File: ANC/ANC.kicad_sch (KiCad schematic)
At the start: 67 parts, among them J1 Screw_Terminal_01x04, J10 Conn_01x03, J11 Conn_01x03, J12 Conn_01x03, J13 Conn_01x03, J3 SJ2-35894B-SMT-TR, J5 Conn_01x04, J7 Conn_01x04, J8 Conn_01x04, J9 Conn_01x04, U1 ICS-40730, U2 MAX98090AETL_T, U3 ICS-40730, U4 CMM-3729AB-38308-TR, U5 CMM-3729AB-38308-TR, U6 TLV172IDCK, U7 TLV172IDCK, Y1 ASE-12.288MHZ-LC-T, x1 0, x2 0

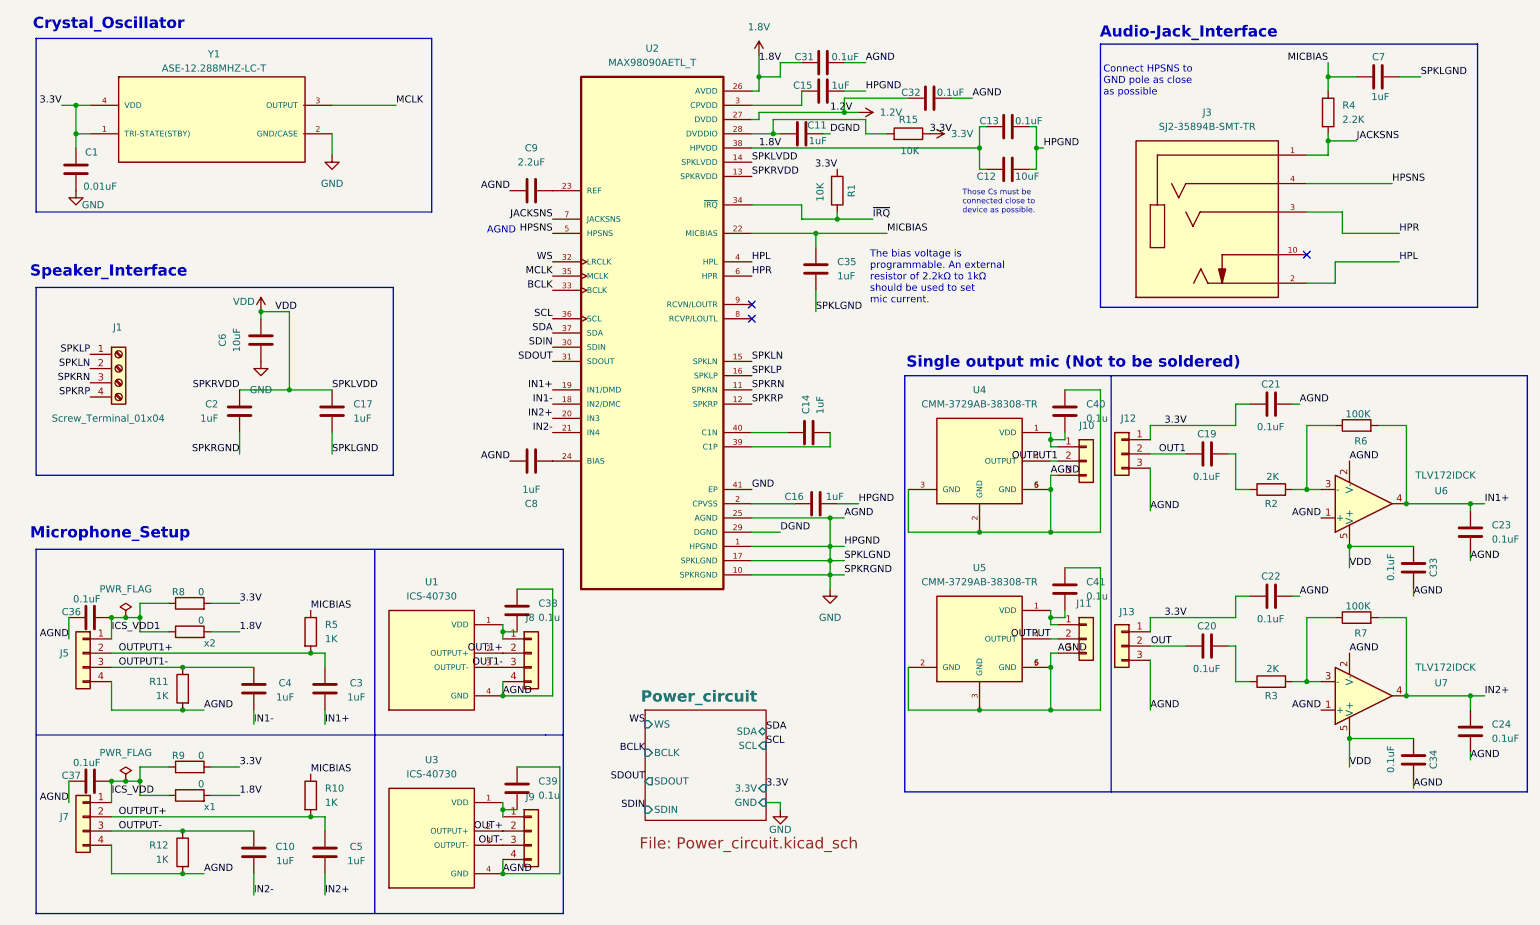
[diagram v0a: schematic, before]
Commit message: Added ANC
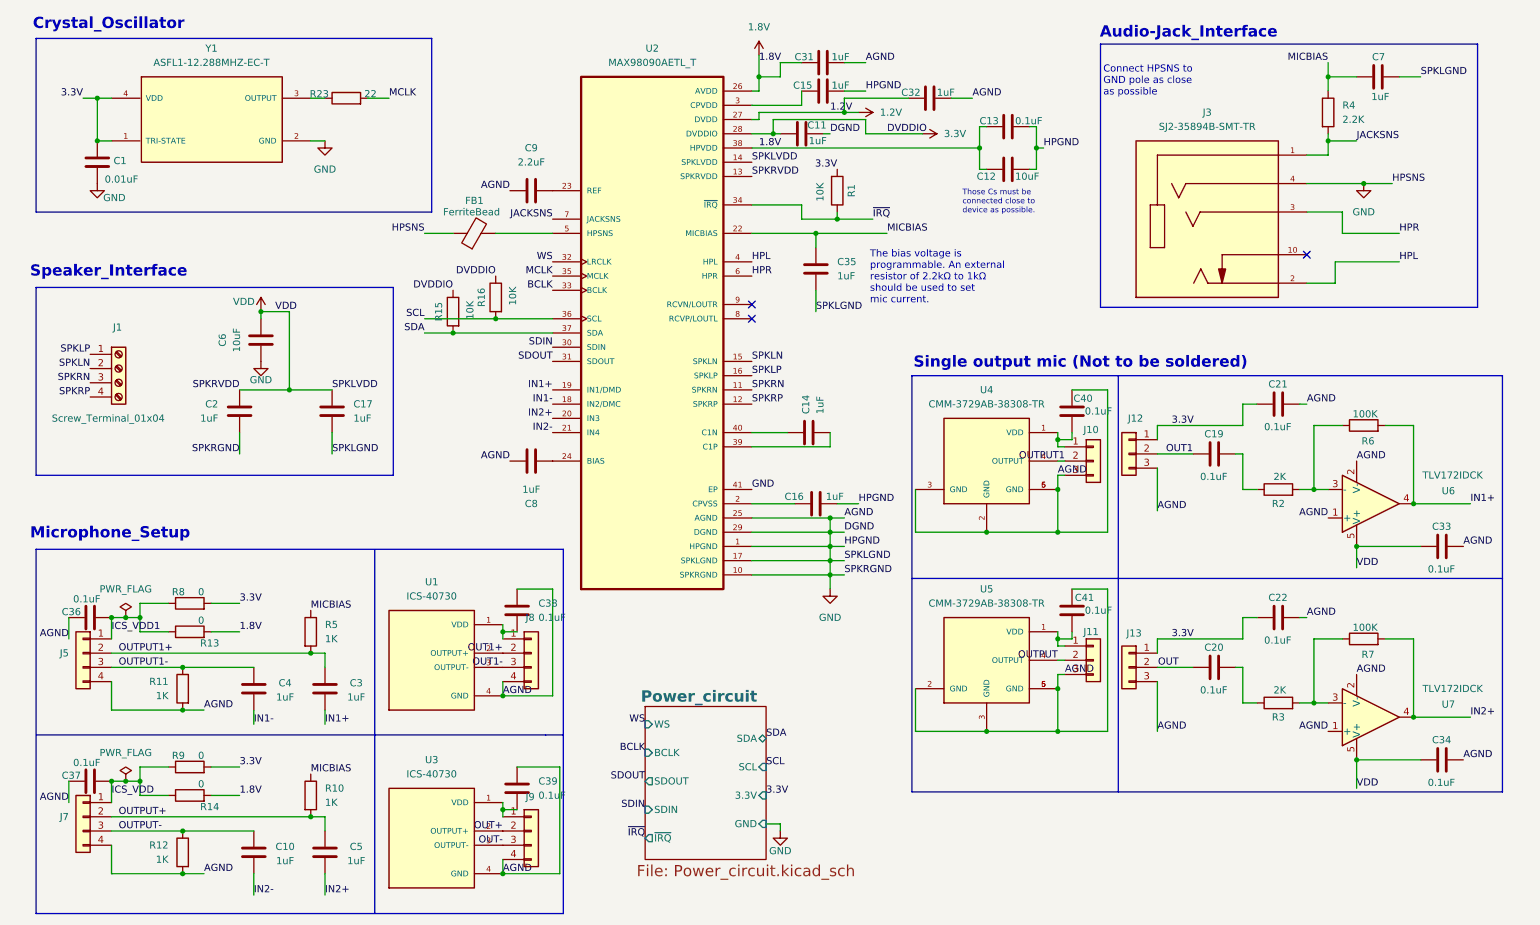
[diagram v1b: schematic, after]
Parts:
- removed C23, C24: 0.1uF, Capacitor_SMD:C_0805_2012Metric_Pad1.18x1.45mm_HandSolder, symbol Device:C
- removed Y1: ASE-12.288MHZ-LC-T, ASE-12.288MHZ-LC-T:XTAL_ASE-12.288MHZ-LC-T, symbol ANC:ASE-12.288MHZ-LC-T
- added FB1: FerriteBead, Inductor_SMD:L_0402_1005Metric, symbol Device:FerriteBead
- added R16: 10K, Resistor_SMD:R_0402_1005Metric_Pad0.72x0.64mm_HandSolder, symbol Device:R
- added R23: 22, Resistor_SMD:R_0402_1005Metric_Pad0.72x0.64mm_HandSolder, symbol Device:R
- added Y1: ASFL1-12.288MHZ-EC-T, ASFL1_12_288MHZ_EC_T:XTAL_ASFL1-12.288MHZ-EC-T, symbol ANC:ASFL1-12.288MHZ-EC-T
- C1, C10, C11, C13, C14, C15, C16, C17, C19, C2, C20, C21, C22, C3, C33, C34, C35, C36, C37, C4, C5, C7, C8: footprint Capacitor_SMD:C_0805_2012Metric_Pad1.18x1.45mm_HandSolder -> Capacitor_SMD:C_0402_1005Metric_Pad0.74x0.62mm_HandSolder
- C31, C32: value 0.1uF -> 1uF; footprint Capacitor_SMD:C_0805_2012Metric_Pad1.18x1.45mm_HandSolder -> Capacitor_SMD:C_0402_1005Metric_Pad0.74x0.62mm_HandSolder
- C38, C39, C40, C41: value 0.1u -> 0.1uF; footprint Capacitor_SMD:C_0805_2012Metric_Pad1.18x1.45mm_HandSolder -> Capacitor_SMD:C_0402_1005Metric_Pad0.74x0.62mm_HandSolder
- renumbered x2 to R13, x1 to R14
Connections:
- net DGND is gone; now on net GND: C11.1, U2.29 (DGND)
- net 3.3V: now also C11.2, U2.28 (DVDDIO), R16.1, Y1.1 (TRI-STATE), Y1.4 (VDD)
- net GND: now also J3.4, FB1.1, Y1.2 (GND)
- net MCLK: now also R23.2
- net SCL: now also R16.2
- net SDA: now also R15.2
- net HPSNS: no longer names the net of U2.5 (HPSNS)
- net HPSNS: now also FB1.2; no longer J3.4
- new net: R23.1, Y1.3 (OUTPUT)
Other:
- sheet Power_circuit ports: added ~{IRQ}; removed none
- note removed: "AGND"
- moved on the sheet: C1, C19, C20, C21, C22, C33, C34, C40, C41, J10, J11, J12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
